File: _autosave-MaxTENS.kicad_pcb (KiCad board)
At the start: 2 copper layers, 49.3 x 69.8 mm, 145 parts, among them IC1 ESP32-WROOM-32E-N8, IC2 AP7366-33W5-7, J2 PJ-040-SMT-TR, J3 20021121-00006C4LF, J4 Conn_01x12, J5 20021121-00010C4LF, J6 Conn_01x02_Pin, J7 PJ-040-SMT-TR, Q1 PMV37ENEAR, Q10 NPN, Q11 PNP, Q12 NPN, Q16 NPN, Q17 PNP, Q18 NPN, Q19 NPN, Q2 NPN, Q20 PNP, Q21 NPN, Q3 NPN, Q4 NPN, Q5 PNP, Q6 NPN, Q7 NPN, Q8 PNP, Q9 NPN, U1 ADA4522-2ARMZ-R7, U10 2N7002KDW_R1_00001, U11 2N7002KDW_R1_00001, U2 PCAL6524HEAZ, U3 MCP73812T-420I/OT, U4 2N7002KDW_R1_00001, U5 2N7002KDW_R1_00001, U6 2N7002KDW_R1_00001, U7 2N7002KDW_R1_00001, U8 2N7002KDW_R1_00001, U9 2N7002KDW_R1_00001

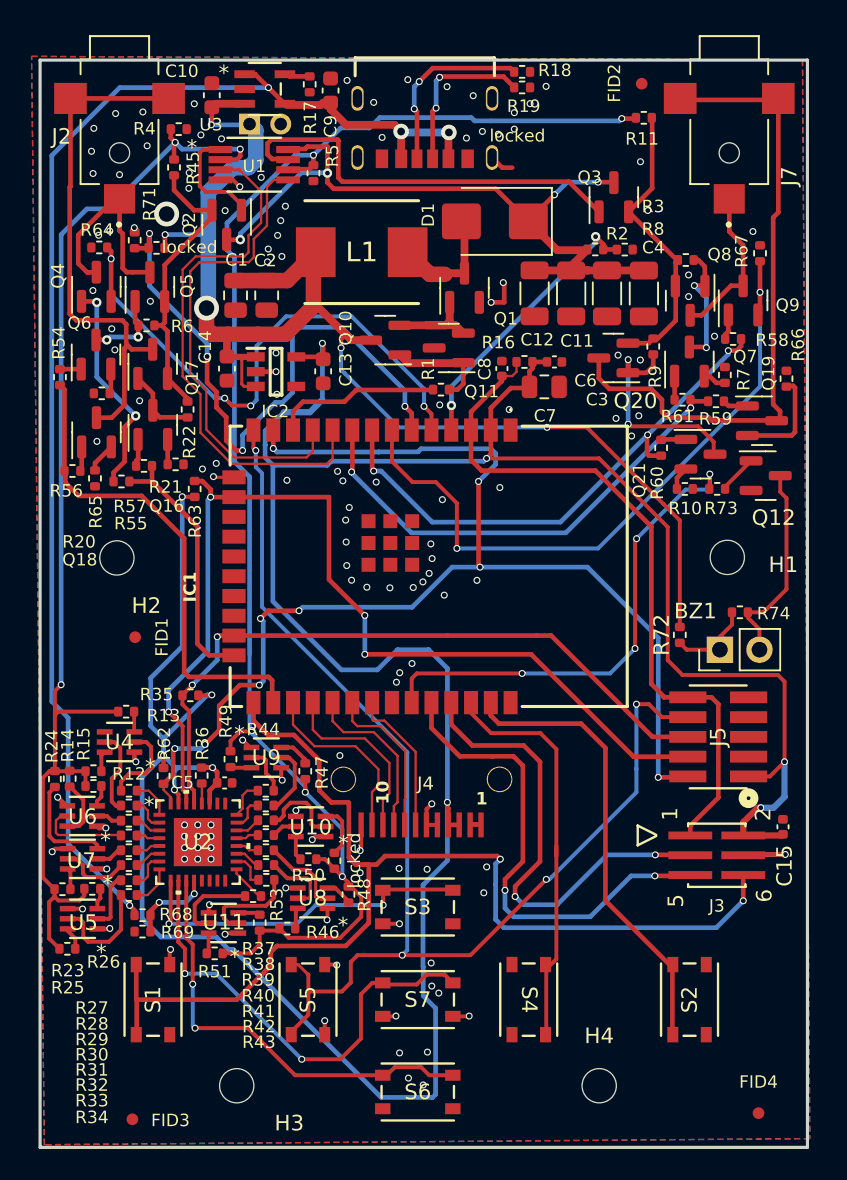
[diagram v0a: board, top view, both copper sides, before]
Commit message: version 5: replaced ESP32-WROVER module with ESP-Mini, removed 2.5mm plugs, changed USB connector and routed electrode signals on it, added RC snubber circuit to boost converter and output caps to reduce switching loop
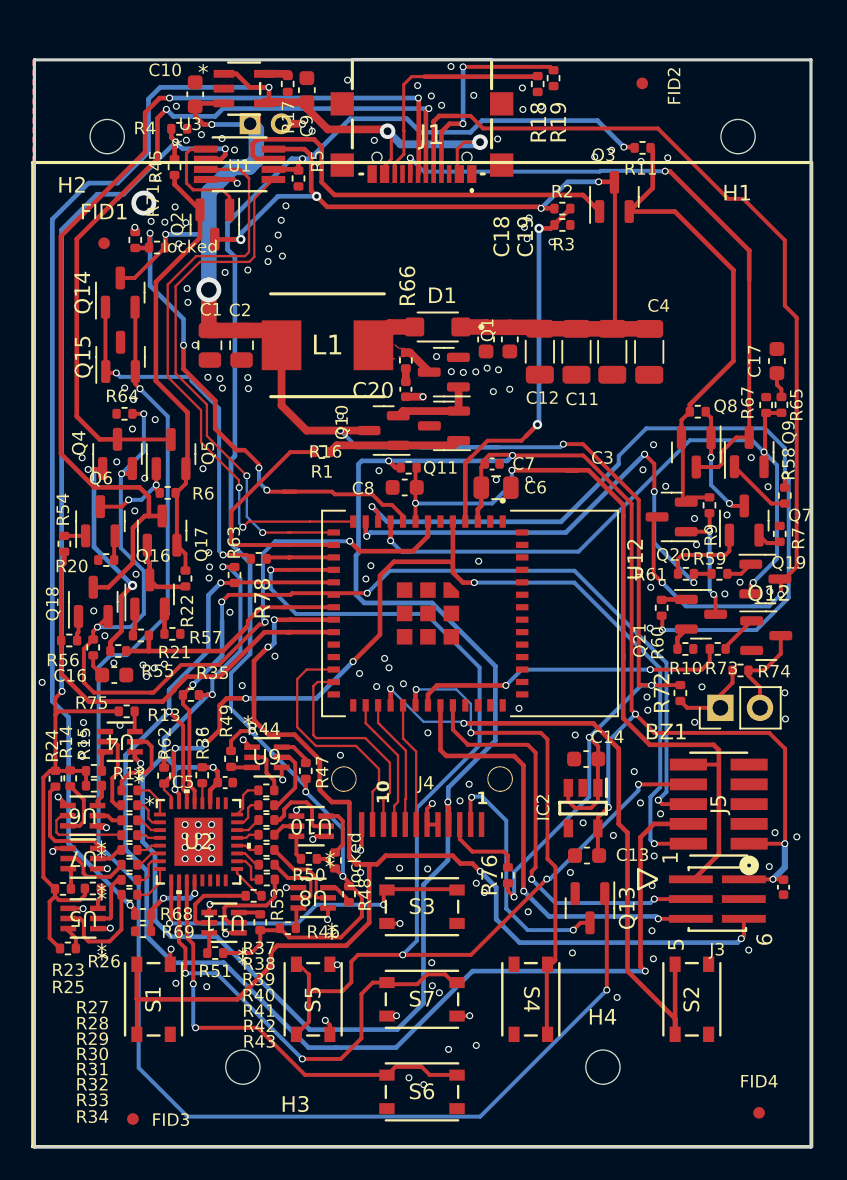
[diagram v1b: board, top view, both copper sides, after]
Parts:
- removed IC1: ESP32-WROOM-32E-N8, Library:ESP32WROOM32EN8
- removed J2, J7: PJ-040-SMT-TR, Library:CUI_PJ-040-SMT-TR
- removed the locked at (223.6, 43.6)
- added C16: 1u, Capacitor_SMD:C_0603_1608Metric, F.Cu at (203.6, 79.8)
- added C17: 1u, Capacitor_SMD:C_0603_1608Metric, F.Cu at (246.2, 59.7)
- added C18: 0.1u, Capacitor_SMD:C_0603_1608Metric, F.Cu at (227.5, 58.3)
- added C19: 10n, Capacitor_SMD:C_0603_1608Metric, F.Cu at (229.0, 58.3)
- added C20: 0.1u, Capacitor_SMD:C_0402_1005Metric, F.Cu at (222.3, 61.5)
- added J1: GSB1C41110SSHR, Library:GSB1C41110SSHR, F.Cu at (223.4, 44.3)
- added Q13: T2N7002BK,LM, Package_TO_SOT_SMD:SOT-23, F.Cu at (234.2, 94.8)
- added Q14: NPN, Package_TO_SOT_SMD:SOT-23, F.Cu at (204.0, 55.3)
- added Q15: PNP, Package_TO_SOT_SMD:SOT-23, F.Cu at (204.0, 59.4)
- added R75: 5k, Resistor_SMD:R_0402_1005Metric, F.Cu at (202.3, 78.1)
- added R76: 10, Resistor_SMD:R_0402_1005Metric, F.Cu at (228.9, 92.7)
- added R78: 100, Resistor_SMD:R_0402_1005Metric, F.Cu at (212.9, 72.4)
- added U12: ESP32-MINI-1-N4, Library:XCVR_ESP32-MINI-1-N4, F.Cu at (223.8, 75.9)
- C6: value 0.1u -> 22u; footprint Capacitor_SMD:C_0402_1005Metric -> Capacitor_SMD:C_0805_2012Metric
- C7: value 22u -> 0.1u; footprint Capacitor_SMD:C_0805_2012Metric -> Capacitor_SMD:C_0402_1005Metric
- C8: value a -> 1u; footprint Capacitor_SMD:C_0402_1005Metric -> Capacitor_SMD:C_0603_1608Metric
- D1: value SK520B -> DSS18UTR; footprint Diode_SMD:D_SMB -> Library:SODFL3618X110N
- R16: value DNP -> 10k
- R3: value 11.5k -> 10k
- R64, R67: value 10 -> 15
- R65: value 10 -> 5k
- R66: value 10 -> 10k
- moved R65 44.3 mm to (246.5, 62.5)
- moved C13 35.4 mm to (234.0, 91.4), turned to 180 degrees
- moved IC2 34.3 mm to (233.7, 88.4), turned to -90 degrees
- moved C14 34.1 mm to (233.9, 85.2), turned to 180 degrees
- moved H2 27.1 mm to (203.2, 45.3)
- moved H1 27.0 mm to (243.7, 45.3)
- moved FID1 25.4 mm to (203.0, 52.1)
- moved R66 24.5 mm to (222.3, 59.6), turned to -90 degrees
- moved R61 11.2 mm to (240.3, 73.3)
- moved R59 11.1 mm to (242.5, 73.3)
- moved Q16 10.9 mm to (205.9, 74.7)
- moved R21 10.9 mm to (207.3, 77.2)
- moved R56 10.9 mm to (200.7, 77.6)
- moved Q18 10.9 mm to (202.3, 75.1)
- moved R57 10.9 mm to (205.3, 77.3)
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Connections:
- net /ElectrodeChannels/CH1_N renamed /BatteryCharger/CH1_N
- net /ElectrodeChannels/CH1_P renamed /BatteryCharger/CH1_P
- net /ElectrodeChannels/CH2_N renamed /BatteryCharger/CH2_N
- net /ElectrodeChannels/CH2_P renamed /BatteryCharger/CH2_P
- C8 pad 1: /MCU/EN -> GND
- C8 pad 2: GND -> /MCU/EN
- J4 pad 2: GND -> /LCD/LCD_K
- J4 pad 3: +3.3V -> /LCD/LCD_A
- L1 pad 2: Net-(D1-A) -> Net-(Q1-D)
- Q1 pad 3: Net-(D1-A) -> Net-(Q1-D)
- Q18 pad 2: Net-(Q18-E) -> /ElectrodeChannels/EL1_DET
- Q19 pad 2: Net-(Q19-E) -> /ElectrodeChannels/EL2_DET
- R65 pad 1: Net-(Q18-E) -> Net-(C17-Pad1)
- R65 pad 2: GND -> /ElectrodeChannels/EL2_DET
- R66 pad 1: Net-(Q19-E) -> Net-(Q1-D)
- R66 pad 2: GND -> Net-(C20-Pad2)
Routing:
- net Net-(Q13-G): track 0.00 -> 94.2 mm, vias 0 -> 2
- net /BatteryCharger/CH1_P: track 13.2 -> 50.3 mm, vias 0 -> 2
- net /BatteryCharger/CH2_P: track 10.0 -> 41.9 mm, vias 0 -> 2
- net /BatteryCharger/CH1_N: track 33.2 -> 62.6 mm, vias 0 -> 2
- net +3.3V: track 205.1 -> 177.3 mm, vias 10 -> 12
- net /BatteryCharger/CH2_N: track 41.8 -> 66.1 mm, vias 0 -> 2
- net Net-(Q14-B): track 0.00 -> 23.9 mm, vias 0 -> 2
- net +BATT: track 87.5 -> 111.4 mm, vias 5 -> 8
- net /MCU/MOSI: track 65.1 -> 88.5 mm, vias 4 -> 3
- net /ElectrodeChannels/CH2_1: track 35.1 -> 51.7 mm
- net /MCU/INT_IO_EXP: track 79.7 -> 63.1 mm, vias 9 -> 6
- net /ElectrodeChannels/EL1_DET: track 38.1 -> 54.6 mm, vias 4 -> 5
- net /LCD/LCD_K: track 0.00 -> 16.0 mm, vias 0 -> 2
- net /MCU/CH2_BTN: track 29.0 -> 41.5 mm, vias 0 -> 2
- net +OUT_2: track 18.7 -> 31.1 mm
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- added copper zone on F.Cu, net Net-(Q1-D)
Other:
- board size 49.3 x 69.8 mm -> 49.9 x 69.8 mm
- board text added: "0.1500 mm / 0.1500 mm"
- board text added: "0.3000 mm"
- board text added: "0.8000 mm"
- board text added: "2"
- board text added: "49.2700 mm x 69.8100 mm"
- board text added: "BOARD CHARACTERISTICS"
- board text added: "Board Thickness:"
- board text added: "Board overall dimensions:"
- board text added: "Castellated pads:"
- board text added: "Copper Finish:"
- board text added: "Copper Layer Count:"
- board text added: "Edge card connectors:"
- board text added: "HAL lead-free"
- board text added: "Impedance Control:"
- board text added: "Min hole diameter:"
- board text added: "Min track/spacing:"
- board text added: "No"
- board text added: "Plated Board Edge:"

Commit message: Fixed electrode detection mechanism, modified position of USB Type-C port
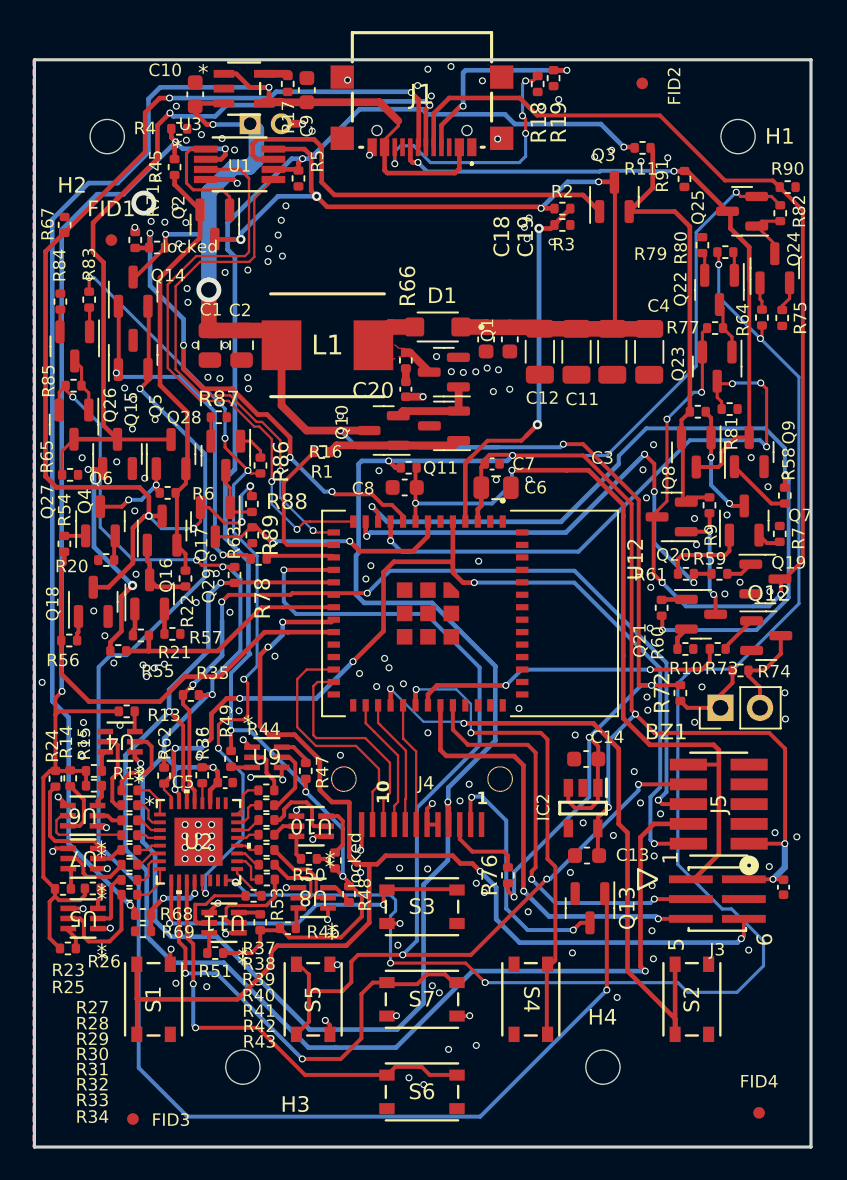
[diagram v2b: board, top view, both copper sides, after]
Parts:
- removed C16, C17: 1u, Capacitor_SMD:C_0603_1608Metric
- added Q22: NPN, Package_TO_SOT_SMD:SOT-23, F.Cu at (242.5, 55.1)
- added Q23: PNP, Package_TO_SOT_SMD:SOT-23, F.Cu at (242.3, 60.0)
- added Q24: NPN, Package_TO_SOT_SMD:SOT-23, F.Cu at (246.0, 53.7)
- added Q25: PNP, Package_TO_SOT_SMD:SOT-23, F.Cu at (243.9, 50.0)
- added Q26: NPN, Package_TO_SOT_SMD:SOT-23, F.Cu at (201.1, 58.7)
- added Q27: PNP, Package_TO_SOT_SMD:SOT-23, F.Cu at (201.0, 63.8)
- added Q28: NPN, Package_TO_SOT_SMD:SOT-23, F.Cu at (210.8, 65.8)
- added Q29: PNP, Package_TO_SOT_SMD:SOT-23, F.Cu at (210.1, 70.0)
- added R77: 100k, Resistor_SMD:R_0402_1005Metric, F.Cu at (242.2, 57.5)
- added R79: 300, Resistor_SMD:R_0402_1005Metric, F.Cu at (242.8, 52.7)
- added R80: 1k, Resistor_SMD:R_0402_1005Metric, F.Cu at (241.4, 52.2)
- added R81: 10k, Resistor_SMD:R_0402_1005Metric, F.Cu at (243.1, 62.8)
- added R82: 100k, Resistor_SMD:R_0402_1005Metric, F.Cu at (246.4, 50.2)
- added R83: 300, Resistor_SMD:R_0402_1005Metric, F.Cu at (202.0, 55.7)
- added R84: 1k, Resistor_SMD:R_0402_1005Metric, F.Cu at (200.2, 55.9)
- added R85: 100k, Resistor_SMD:R_0402_1005Metric, F.Cu at (201.0, 61.2)
- added R86: 300, Resistor_SMD:R_0402_1005Metric, F.Cu at (213.0, 66.4)
- added R87: 1k, Resistor_SMD:R_0402_1005Metric, F.Cu at (210.3, 63.3)
- added R88: 100k, Resistor_SMD:R_0402_1005Metric, F.Cu at (212.4, 68.8)
- added R89: 10k, Resistor_SMD:R_0402_1005Metric, F.Cu at (212.5, 70.8)
- added R90: 1M, Resistor_SMD:R_0402_1005Metric, F.Cu at (246.8, 48.5)
- added R91: 1M, Resistor_SMD:R_0402_1005Metric, F.Cu at (240.2, 48.0)
- R64: value 15 -> 300
- R65: value 5k -> 1M
- R67: value 15 -> 1M
- R75: value 5k -> 1k
- moved R75 49.0 mm to (246.5, 56.9), turned to -90 degrees
- moved R67 46.5 mm to (200.4, 50.9)
- moved R65 45.9 mm to (200.8, 67.0), turned to 0 degrees
- moved R64 41.4 mm to (245.2, 56.9), turned to 90 degrees
- moved J1 1.72 mm to (223.4, 42.5)
- moved Q14 0.83 mm to (204.8, 55.2)
- moved Q15 0.82 mm to (204.8, 59.3)
- moved FID1 0.51 mm to (203.4, 51.9)
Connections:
- Q18 pad 2: /ElectrodeChannels/EL1_DET -> GND
- Q19 pad 2: /ElectrodeChannels/EL2_DET -> GND
- Q4 pad 2: /ElectrodeChannels/EL1_DET -> GND
- Q9 pad 2: /ElectrodeChannels/EL2_DET -> GND
- R64 pad 1: /ElectrodeChannels/EL1_DET -> /ElectrodeChannels/CH2_EL_DET
- R64 pad 2: GND -> Net-(Q24-B)
- R65 pad 1: Net-(C17-Pad1) -> /BatteryCharger/CH1_P
- R65 pad 2: /ElectrodeChannels/EL2_DET -> GND
- R67 pad 1: /ElectrodeChannels/EL2_DET -> /BatteryCharger/CH1_N
- R75 pad 2: /ElectrodeChannels/EL1_DET -> GND
- U2 pad 13: unconnected-(U2-P1_4-Pad13) -> /ElectrodeChannels/CH1_EL_DET
- U2 pad 16: unconnected-(U2-P1_7-Pad16) -> /ElectrodeChannels/CH2_EL_DET
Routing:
- net /ElectrodeChannels/CH2_EL_DET: track 0.00 -> 97.3 mm, vias 0 -> 5
- net /ElectrodeChannels/CH1_EL_DET: track 0.00 -> 51.3 mm, vias 0 -> 6
- net +3.3V: track 177.3 -> 227.5 mm, vias 12 -> 15
- net /ElectrodeChannels/EL1_DET: track 54.6 -> 15.9 mm, vias 5 -> 2
- net /BatteryCharger/CH2_N: track 66.1 -> 81.4 mm, vias 2 -> 4
- net /BatteryCharger/CH1_N: track 62.6 -> 74.4 mm, vias 2 -> 6
- net /BoostConverter/VSW: track 15.8 -> 9.84 mm
- net /ElectrodeChannels/EL2_DET: track 43.4 -> 37.9 mm, vias 3 -> 4
- net Net-(Q28-C): track 0.00 -> 3.97 mm
- net Net-(Q24-C): track 0.00 -> 3.90 mm
- net Net-(Q26-C): track 0.00 -> 3.52 mm
- net Net-(Q22-C): track 0.00 -> 3.38 mm
- net +5V: track 93.3 -> 90.7 mm, vias 4 -> 2
- net +OUT_2: track 31.1 -> 28.8 mm
- net /BatteryCharger/CH1_P: track 50.3 -> 52.5 mm
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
